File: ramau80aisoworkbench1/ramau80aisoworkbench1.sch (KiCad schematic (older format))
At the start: 16 parts, among them J1 USB_mini_micro_B, SW1 SW_PUSH, U1 ATMEGA32U4, X1 XTAL_GND

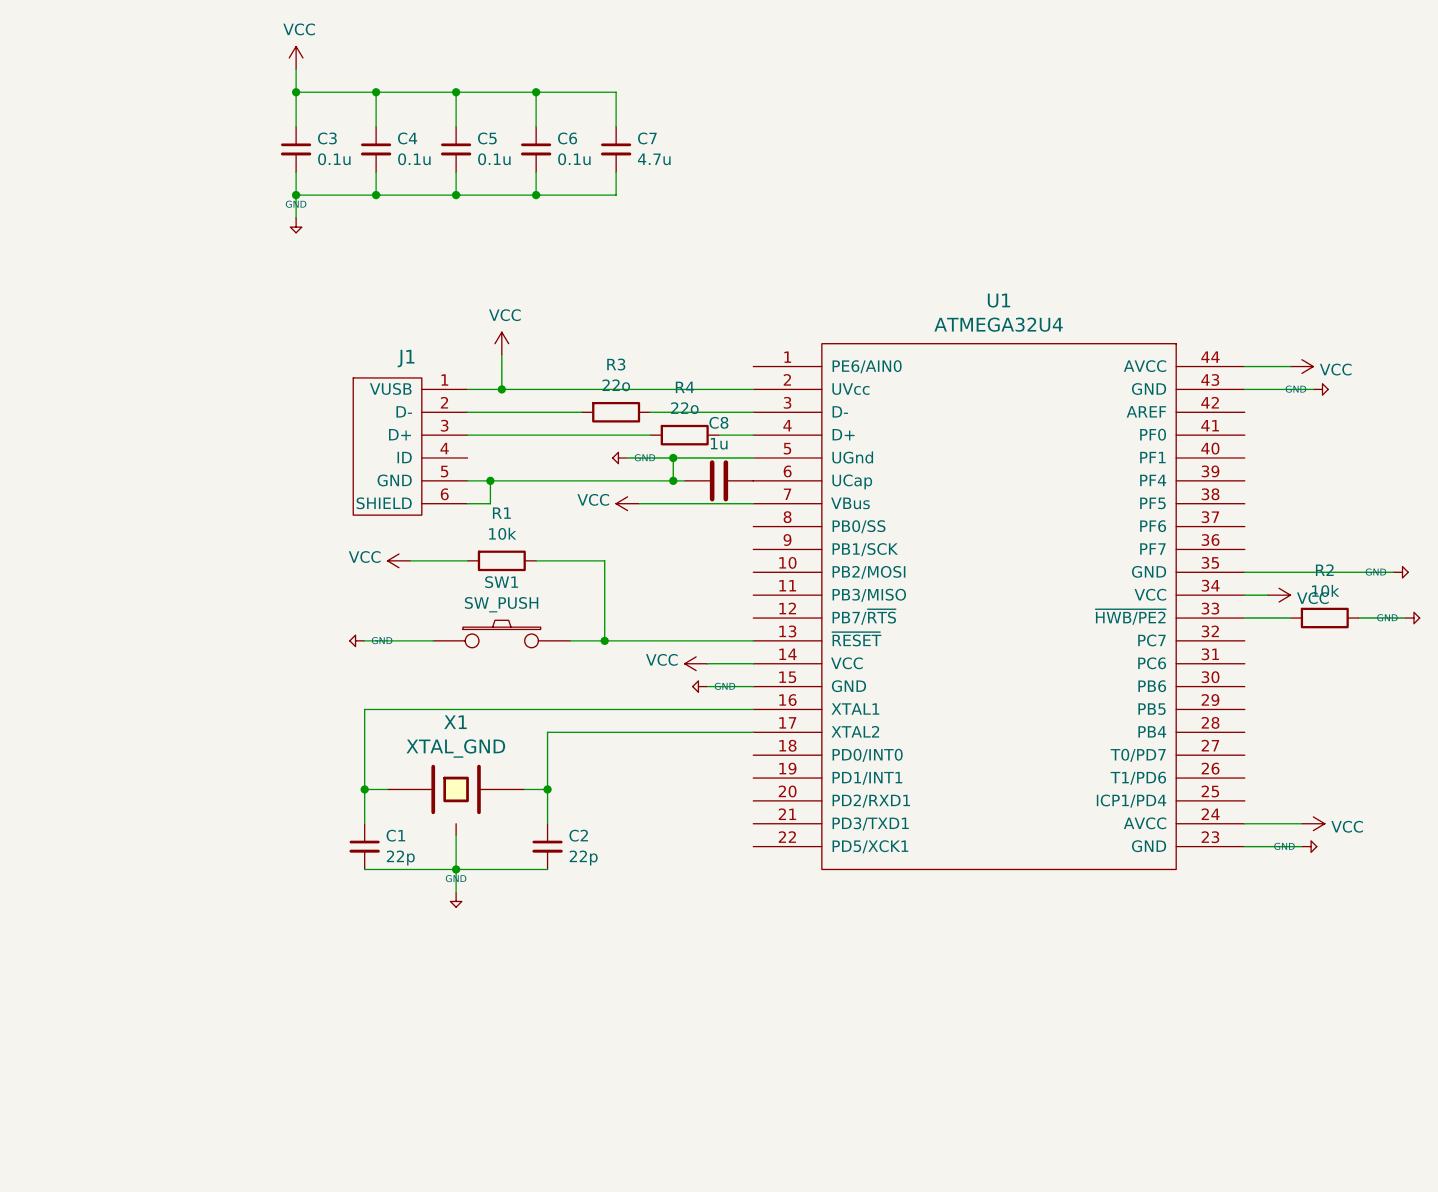
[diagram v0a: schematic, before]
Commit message: starting schematic over following ai03 instructions... lets see. todo, turn usb mini-b into usb-c later...
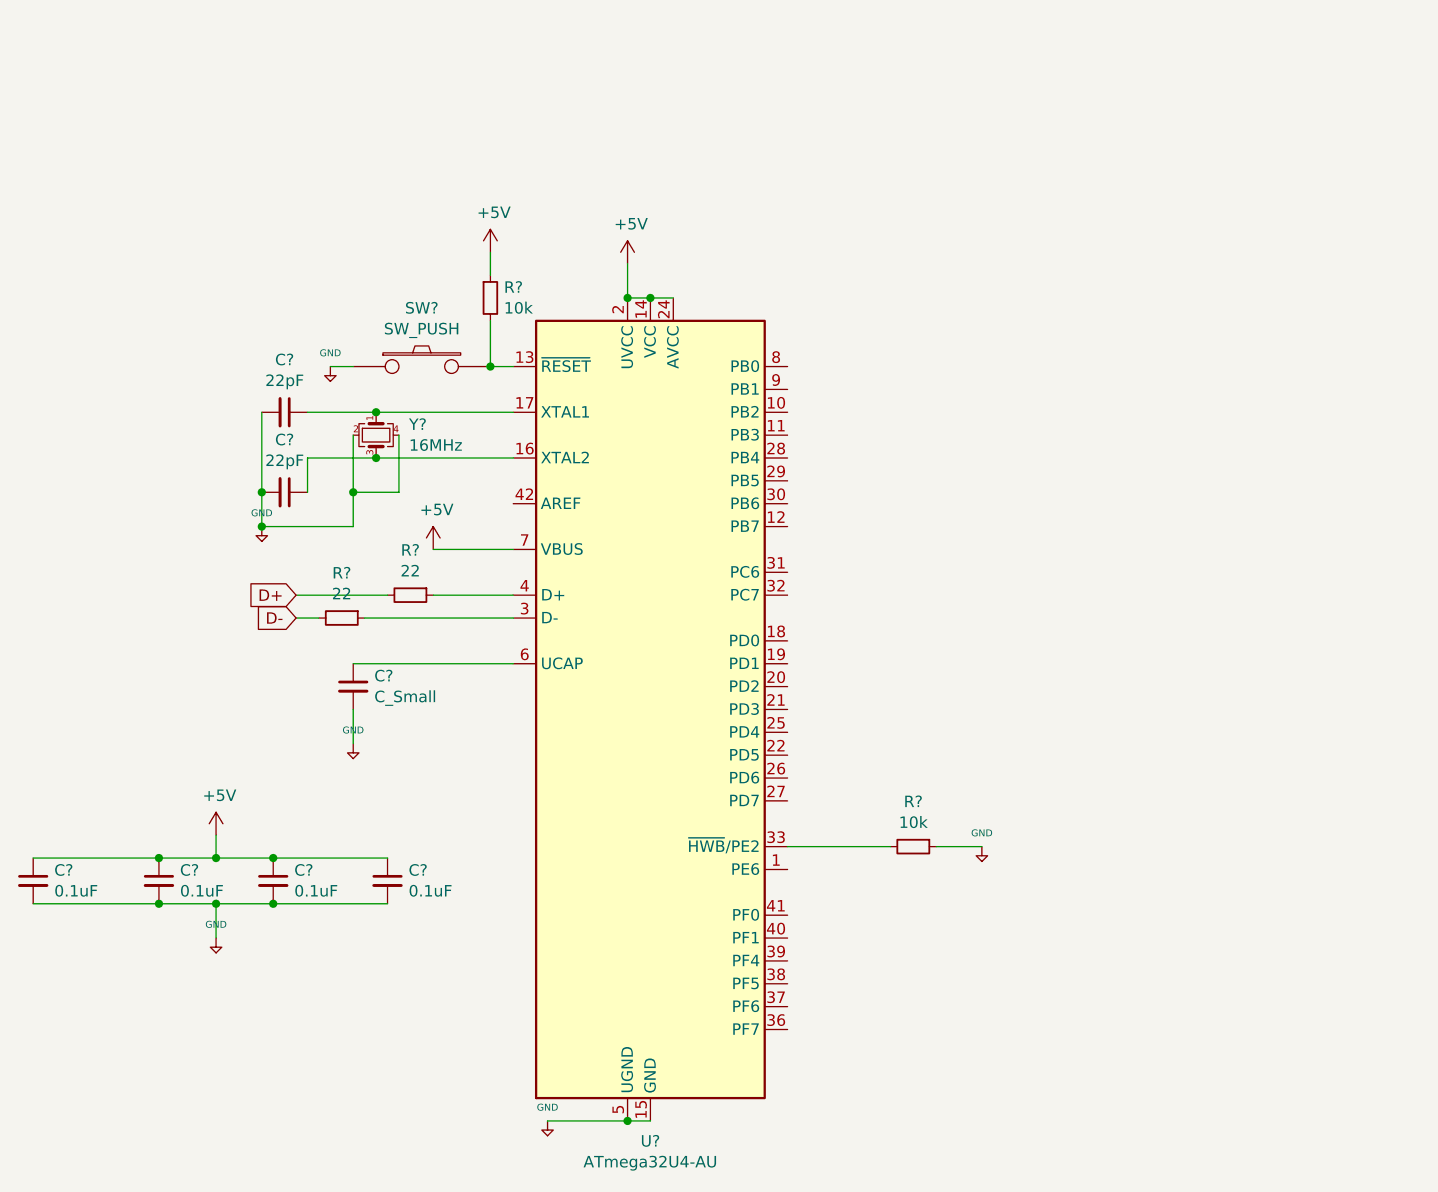
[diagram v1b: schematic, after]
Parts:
- removed C1, C2: 22p, symbol Device:C_Small
- removed C3, C4, C5, C6: 0.1u, symbol Device:C_Small
- removed C7: 4.7u, symbol Device:C_Small
- removed C8: 1u, symbol Device:C
- removed J1: USB_mini_micro_B, symbol keyboard_parts:USB_mini_micro_B
- removed R1, R2: 10k, symbol Device:R
- removed R3, R4: 22o, symbol Device:R
- removed SW1: SW_PUSH, symbol keyboard_parts:SW_PUSH
- removed U1: ATMEGA32U4, symbol keyboard_parts:ATMEGA32U4
- removed X1: XTAL_GND, symbol keyboard_parts:XTAL_GND
- added C?: C_Small, symbol Device:C_Small
- added C? (x4): 0.1uF, symbol Device:C_Small
- added C? (x2): 22pF, symbol Device:C_Small
- added R? (x2): 10k, symbol Device:R_Small
- added R? (x2): 22, symbol Device:R_Small
- added SW?: SW_PUSH, symbol keyboard_parts:SW_PUSH
- added U?: ATmega32U4-AU, Package_QFP:TQFP-44_10x10mm_P0.8mm, symbol MCU_Microchip_ATmega:ATmega32U4-AU
- added Y?: 16MHz, symbol Device:Crystal_GND24_Small
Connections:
- net +5V: now also C?.1, C?.1, C?.1, C?.1, C?.2, C?.2, C?.2, C?.2, C?.2, C?.2, C?.2, R?.1, R?.1, SW?.1, U?.14 (VCC), U?.15 (GND), U?.2 (UVCC), U?.23 (GND), U?.24 (AVCC), U?.34 (VCC), U?.35 (GND), U?.43 (GND), U?.44 (AVCC), U?.5 (UGND), U?.7 (VBUS), Y?.2, Y?.4
- new net: R?.2, SW?.2, U?.13 (~RESET)
- new net: C?.1, U?.16 (XTAL2), Y?.3
- new net: C?.1, U?.17 (XTAL1), Y?.1
- new net: R?.1, U?.3 (D-)
- new net: R?.2, U?.33 (~HWB~/PE2)
- new net: R?.1, U?.4 (D+)
- new net: C?.1, U?.6 (UCAP)
- new net D+: R?.2
- new net D-: R?.2

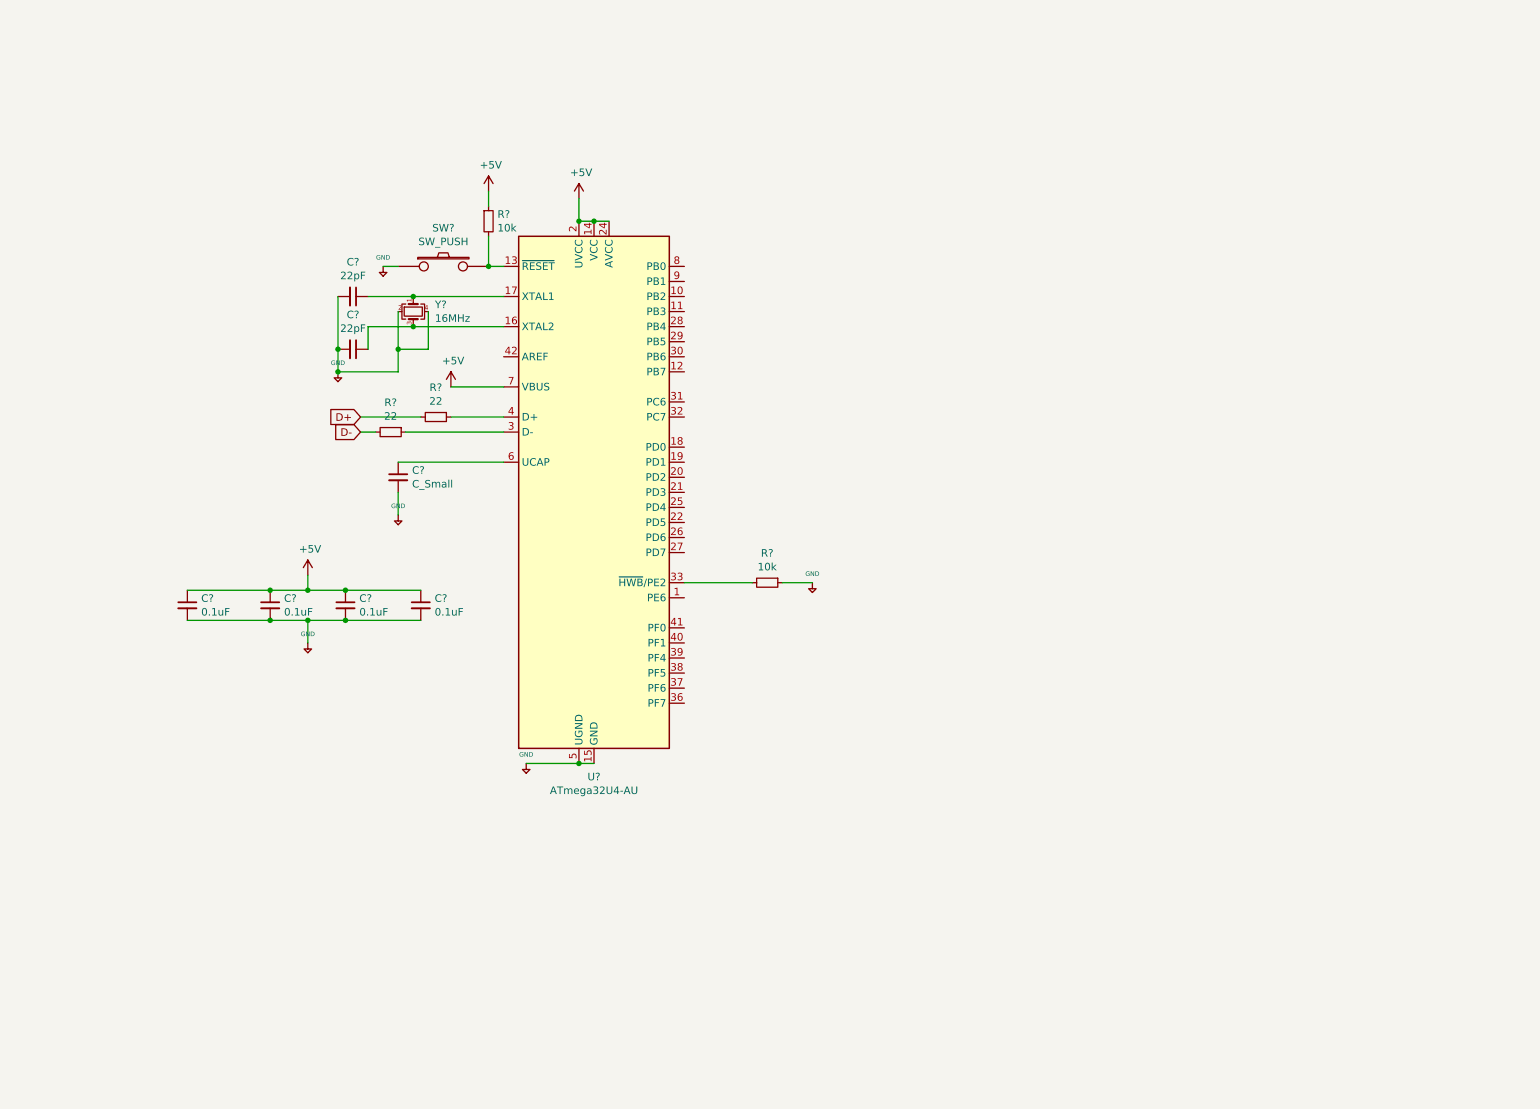
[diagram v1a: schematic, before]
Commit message: grid complete. probs need more capacitors.
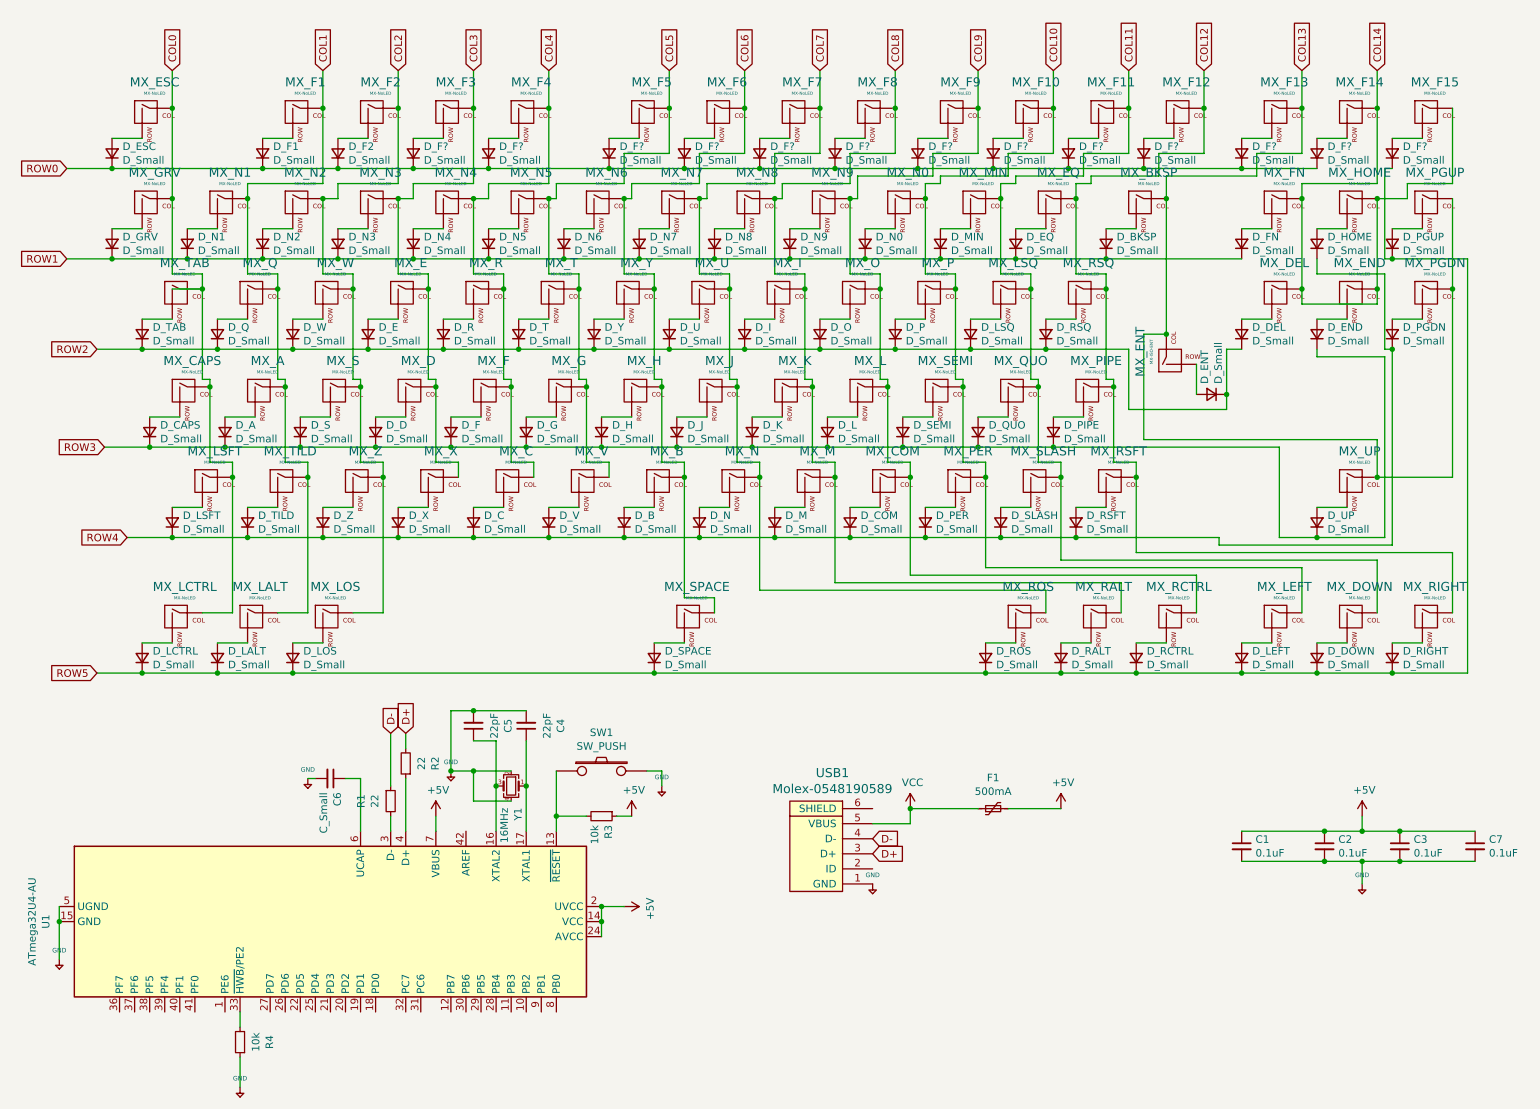
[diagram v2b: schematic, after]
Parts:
- added D_A, D_B, D_BKSP, D_C, D_CAPS, D_COM, D_D, D_DEL, D_DOWN, D_E, D_END, D_ENT, D_EQ, D_ESC, D_F, D_F1, D_F2, D_F? (x13), D_FN, D_G, D_GRV, D_H, D_HOME, D_I, D_J, D_K, D_L, D_LALT, D_LCTRL, D_LEFT, D_LOS, D_LSFT, D_LSQ, D_M, D_MIN, D_N, D_N0, D_N1, D_N2, D_N3, D_N4, D_N5, D_N6, D_N7, D_N8, D_N9, D_O, D_P, D_PER, D_PGDN, D_PGUP, D_PIPE, D_Q, D_QUO, D_R, D_RALT, D_RCTRL, D_RIGHT, D_ROS, D_RSFT, D_RSQ, D_S, D_SEMI, D_SLASH, D_SPACE, D_T, D_TAB, D_TILD, D_U, D_UP, D_V, D_W, D_X, D_Y, D_Z: D_Small, Diode_SMD:D_SOD-123, symbol Device:D_Small
- added F1: 500mA, Fuse:Fuse_1206_3216Metric, symbol Device:Polyfuse_Small
- added MX_A, MX_B, MX_BKSP, MX_C, MX_CAPS, MX_COM, MX_D, MX_DEL, MX_DOWN, MX_E, MX_END, MX_EQ, MX_ESC, MX_F, MX_F1, MX_F10, MX_F11, MX_F12, MX_F13, MX_F14, MX_F15, MX_F2, MX_F3, MX_F4, MX_F5, MX_F6, MX_F7, MX_F8, MX_F9, MX_FN, MX_G, MX_GRV, MX_H, MX_HOME, MX_I, MX_J, MX_K, MX_L, MX_LALT, MX_LCTRL, MX_LEFT, MX_LOS, MX_LSFT, MX_LSQ, MX_M, MX_MIN, MX_N, MX_N0, MX_N1, MX_N2, MX_N3, MX_N4, MX_N5, MX_N6, MX_N7, MX_N8, MX_N9, MX_O, MX_P, MX_PER, MX_PGDN, MX_PGUP, MX_PIPE, MX_Q, MX_QUO, MX_R, MX_RALT, MX_RCTRL, MX_RIGHT, MX_ROS, MX_RSFT, MX_RSQ, MX_S, MX_SEMI, MX_SLASH, MX_SPACE, MX_T, MX_TAB, MX_TILD, MX_U, MX_UP, MX_V, MX_W, MX_X, MX_Y, MX_Z: MX-NoLED, MX_Only:MXOnly-1U, symbol MX_Alps_Hybrid:MX-NoLED
- added MX_ENT: MX-ISO-ENT, MX_Only:MXOnly-1U, symbol MX_Alps_Hybrid:MX-NoLED
- added USB1: Molex-0548190589, random-keyboard-parts:PJ-3200B-4A-Assembly, symbol random-keyboard-parts:Molex-0548190589
- C1, C2, C3, C4, C5, C6, C7: renamed from C?; footprint (none) -> Capacitor_SMD:C_0805_2012Metric
- R1, R2, R3, R4: renamed from R?; footprint (none) -> Resistor_SMD:R_0805_2012Metric
- SW1: renamed from SW?; footprint (none) -> random-keyboard-parts:SKQG-1155865
- Y1: renamed from Y?; footprint (none) -> Crystal:Crystal_SMD_3225-4Pin_3.2x2.5mm
- gave numbers to parts that had none: 1
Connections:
- net +5V: now also SW1.2, F1.2, USB1.1 (GND); no longer SW1.1
- net D+: now also USB1.3 (D+)
- net D-: now also R1.1, USB1.4 (D-); no longer R1.2
- net at R3.2, U1.13 (~RESET): now also SW1.1; no longer SW1.2
- net at U1.3 (D-): now also R1.2; no longer R1.1
- new net: D_ESC.2 (A), MX_ESC.2 (ROW)
- new net: D_F1.2 (A), MX_F1.2 (ROW)
- new net: D_GRV.2 (A), MX_GRV.2 (ROW)
- new net: D_F2.2 (A), MX_F2.2 (ROW)
- new net: D_F?.2 (A), MX_F3.2 (ROW)
- new net: D_F?.2 (A), MX_F4.2 (ROW)
- new net: D_F?.2 (A), MX_F5.2 (ROW)
- new net: D_F?.2 (A), MX_F6.2 (ROW)
- new net: D_F?.2 (A), MX_F7.2 (ROW)
- new net: D_F?.2 (A), MX_F8.2 (ROW)
- new net: D_F?.2 (A), MX_F9.2 (ROW)
- new net: D_F?.2 (A), MX_F10.2 (ROW)
- new net: D_F?.2 (A), MX_F11.2 (ROW)
- new net: D_F?.2 (A), MX_F12.2 (ROW)
- new net: D_F?.2 (A), MX_F13.2 (ROW)
- new net: D_F?.2 (A), MX_F14.2 (ROW)
- new net: D_F?.2 (A), MX_F15.2 (ROW)
- new net: D_N1.2 (A), MX_N1.2 (ROW)
- new net: D_N2.2 (A), MX_N2.2 (ROW)
- new net: D_N3.2 (A), MX_N3.2 (ROW)
- new net: D_N4.2 (A), MX_N4.2 (ROW)
- new net: D_N5.2 (A), MX_N5.2 (ROW)
- new net: D_N6.2 (A), MX_N6.2 (ROW)
- new net: D_N7.2 (A), MX_N7.2 (ROW)
- new net: D_N8.2 (A), MX_N8.2 (ROW)
- new net: D_N9.2 (A), MX_N9.2 (ROW)
- new net: D_N0.2 (A), MX_N0.2 (ROW)
- new net: D_MIN.2 (A), MX_MIN.2 (ROW)
- new net: D_EQ.2 (A), MX_EQ.2 (ROW)
- new net: D_BKSP.2 (A), MX_BKSP.2 (ROW)
- new net: D_FN.2 (A), MX_FN.2 (ROW)
- new net: D_HOME.2 (A), MX_HOME.2 (ROW)
- new net: D_PGUP.2 (A), MX_PGUP.2 (ROW)
- new net: D_TAB.2 (A), MX_TAB.2 (ROW)
- new net: D_Q.2 (A), MX_Q.2 (ROW)
- new net: D_W.2 (A), MX_W.2 (ROW)
- new net: D_E.2 (A), MX_E.2 (ROW)
- new net: D_R.2 (A), MX_R.2 (ROW)
- new net: D_T.2 (A), MX_T.2 (ROW)
- new net: D_Y.2 (A), MX_Y.2 (ROW)
- new net: D_U.2 (A), MX_U.2 (ROW)
- new net: D_I.2 (A), MX_I.2 (ROW)
- new net: D_O.2 (A), MX_O.2 (ROW)
- new net: D_P.2 (A), MX_P.2 (ROW)
- new net: D_LSQ.2 (A), MX_LSQ.2 (ROW)
- new net: D_RSQ.2 (A), MX_RSQ.2 (ROW)
- new net: D_ENT.2 (A), MX_ENT.2 (ROW)
- new net: D_DEL.2 (A), MX_DEL.2 (ROW)
- new net: D_END.2 (A), MX_END.2 (ROW)
- new net: D_PGDN.2 (A), MX_PGDN.2 (ROW)
- new net: D_CAPS.2 (A), MX_CAPS.2 (ROW)
- new net: D_A.2 (A), MX_A.2 (ROW)
- new net: D_S.2 (A), MX_S.2 (ROW)
- new net: D_D.2 (A), MX_D.2 (ROW)
- new net: D_F.2 (A), MX_F.2 (ROW)
- new net: D_G.2 (A), MX_G.2 (ROW)
- new net: D_H.2 (A), MX_H.2 (ROW)
- new net: D_J.2 (A), MX_J.2 (ROW)
- new net: D_K.2 (A), MX_K.2 (ROW)
- new net: D_L.2 (A), MX_L.2 (ROW)
- new net: D_SEMI.2 (A), MX_SEMI.2 (ROW)
- new net: D_QUO.2 (A), MX_QUO.2 (ROW)
- new net: D_PIPE.2 (A), MX_PIPE.2 (ROW)
- new net: D_LSFT.2 (A), MX_LSFT.2 (ROW)
- new net: D_Z.2 (A), MX_Z.2 (ROW)
- new net: D_X.2 (A), MX_X.2 (ROW)
- new net: D_C.2 (A), MX_C.2 (ROW)
- new net: D_V.2 (A), MX_V.2 (ROW)
- new net: D_B.2 (A), MX_B.2 (ROW)
- new net: D_N.2 (A), MX_N.2 (ROW)
- new net: D_M.2 (A), MX_M.2 (ROW)
- new net: D_COM.2 (A), MX_COM.2 (ROW)
- new net: D_PER.2 (A), MX_PER.2 (ROW)
- new net: D_SLASH.2 (A), MX_SLASH.2 (ROW)
- new net: D_RSFT.2 (A), MX_RSFT.2 (ROW)
- new net: D_TILD.2 (A), MX_TILD.2 (ROW)
- new net: D_UP.2 (A), MX_UP.2 (ROW)
- new net: D_LCTRL.2 (A), MX_LCTRL.2 (ROW)
- new net: D_LOS.2 (A), MX_LOS.2 (ROW)
- new net: D_SPACE.2 (A), MX_SPACE.2 (ROW)
- new net: D_ROS.2 (A), MX_ROS.2 (ROW)
- new net: D_RALT.2 (A), MX_RALT.2 (ROW)
- new net: D_RCTRL.2 (A), MX_RCTRL.2 (ROW)
- new net: D_LEFT.2 (A), MX_LEFT.2 (ROW)
- new net: D_DOWN.2 (A), MX_DOWN.2 (ROW)
- new net: D_RIGHT.2 (A), MX_RIGHT.2 (ROW)
- new net: D_LALT.2 (A), MX_LALT.2 (ROW)
- new net COL0: MX_CAPS.1 (COL), MX_ESC.1 (COL), MX_GRV.1 (COL), MX_LCTRL.1 (COL), MX_LSFT.1 (COL), MX_TAB.1 (COL)
- new net COL1: MX_A.1 (COL), MX_F1.1 (COL), MX_LALT.1 (COL), MX_N1.1 (COL), MX_Q.1 (COL), MX_TILD.1 (COL)
- new net COL10: MX_F10.1 (COL), MX_LEFT.1 (COL), MX_N0.1 (COL), MX_P.1 (COL), MX_PER.1 (COL), MX_SEMI.1 (COL)
- new net COL11: MX_DOWN.1 (COL), MX_F11.1 (COL), MX_LSQ.1 (COL), MX_MIN.1 (COL), MX_QUO.1 (COL), MX_SLASH.1 (COL)
- new net COL12: MX_EQ.1 (COL), MX_F12.1 (COL), MX_PIPE.1 (COL), MX_RIGHT.1 (COL), MX_RSFT.1 (COL), MX_RSQ.1 (COL)
- new net COL13: MX_BKSP.1 (COL), MX_ENT.1 (COL), MX_F13.1 (COL), MX_PGDN.1 (COL), MX_PGUP.1 (COL), MX_UP.1 (COL)
- new net COL14: MX_DEL.1 (COL), MX_END.1 (COL), MX_F14.1 (COL), MX_F15.1 (COL), MX_FN.1 (COL), MX_HOME.1 (COL)
- new net COL2: MX_F2.1 (COL), MX_LOS.1 (COL), MX_N2.1 (COL), MX_S.1 (COL), MX_W.1 (COL), MX_Z.1 (COL)
- new net COL3: MX_D.1 (COL), MX_E.1 (COL), MX_F3.1 (COL), MX_N3.1 (COL), MX_X.1 (COL)
- new net COL4: MX_C.1 (COL), MX_F.1 (COL), MX_F4.1 (COL), MX_N4.1 (COL), MX_R.1 (COL)
- new net COL5: MX_F5.1 (COL), MX_G.1 (COL), MX_N5.1 (COL), MX_T.1 (COL), MX_V.1 (COL)
- new net COL6: MX_B.1 (COL), MX_F6.1 (COL), MX_H.1 (COL), MX_N6.1 (COL), MX_SPACE.1 (COL), MX_Y.1 (COL)
- new net COL7: MX_F7.1 (COL), MX_J.1 (COL), MX_N.1 (COL), MX_N7.1 (COL), MX_ROS.1 (COL), MX_U.1 (COL)
- new net COL8: MX_F8.1 (COL), MX_I.1 (COL), MX_K.1 (COL), MX_M.1 (COL), MX_N8.1 (COL), MX_RALT.1 (COL)
- new net COL9: MX_COM.1 (COL), MX_F9.1 (COL), MX_L.1 (COL), MX_N9.1 (COL), MX_O.1 (COL), MX_RCTRL.1 (COL)
- new net ROW0: D_ESC.1 (K), D_F1.1 (K), D_F2.1 (K), D_F?.1 (K), D_F?.1 (K), D_F?.1 (K), D_F?.1 (K), D_F?.1 (K), D_F?.1 (K), D_F?.1 (K), D_F?.1 (K), D_F?.1 (K), D_F?.1 (K), D_F?.1 (K), D_F?.1 (K)
- new net ROW1: D_BKSP.1 (K), D_EQ.1 (K), D_FN.1 (K), D_GRV.1 (K), D_MIN.1 (K), D_N0.1 (K), D_N1.1 (K), D_N2.1 (K), D_N3.1 (K), D_N4.1 (K), D_N5.1 (K), D_N6.1 (K), D_N7.1 (K), D_N8.1 (K), D_N9.1 (K)
- new net ROW2: D_DEL.1 (K), D_E.1 (K), D_ENT.1 (K), D_I.1 (K), D_LSQ.1 (K), D_O.1 (K), D_P.1 (K), D_Q.1 (K), D_R.1 (K), D_RSQ.1 (K), D_T.1 (K), D_TAB.1 (K), D_U.1 (K), D_W.1 (K), D_Y.1 (K)
- new net ROW3: D_A.1 (K), D_CAPS.1 (K), D_D.1 (K), D_END.1 (K), D_F.1 (K), D_G.1 (K), D_H.1 (K), D_J.1 (K), D_K.1 (K), D_L.1 (K), D_PIPE.1 (K), D_QUO.1 (K), D_S.1 (K), D_SEMI.1 (K), D_UP.1 (K)
- new net ROW4: D_B.1 (K), D_C.1 (K), D_COM.1 (K), D_HOME.1 (K), D_LSFT.1 (K), D_M.1 (K), D_N.1 (K), D_PER.1 (K), D_PGDN.1 (K), D_RSFT.1 (K), D_SLASH.1 (K), D_TILD.1 (K), D_V.1 (K), D_X.1 (K), D_Z.1 (K)
- new net ROW5: D_DOWN.1 (K), D_F?.1 (K), D_LALT.1 (K), D_LCTRL.1 (K), D_LEFT.1 (K), D_LOS.1 (K), D_PGUP.1 (K), D_RALT.1 (K), D_RCTRL.1 (K), D_RIGHT.1 (K), D_ROS.1 (K), D_SPACE.1 (K)
- new net VCC: F1.1, USB1.5 (VBUS)
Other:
- moved on the sheet: C1, C2, C3, C4, C5, C6, C7, R1, R2, R3, R4, SW1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
